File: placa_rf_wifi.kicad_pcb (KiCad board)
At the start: 2 copper layers, 9 parts

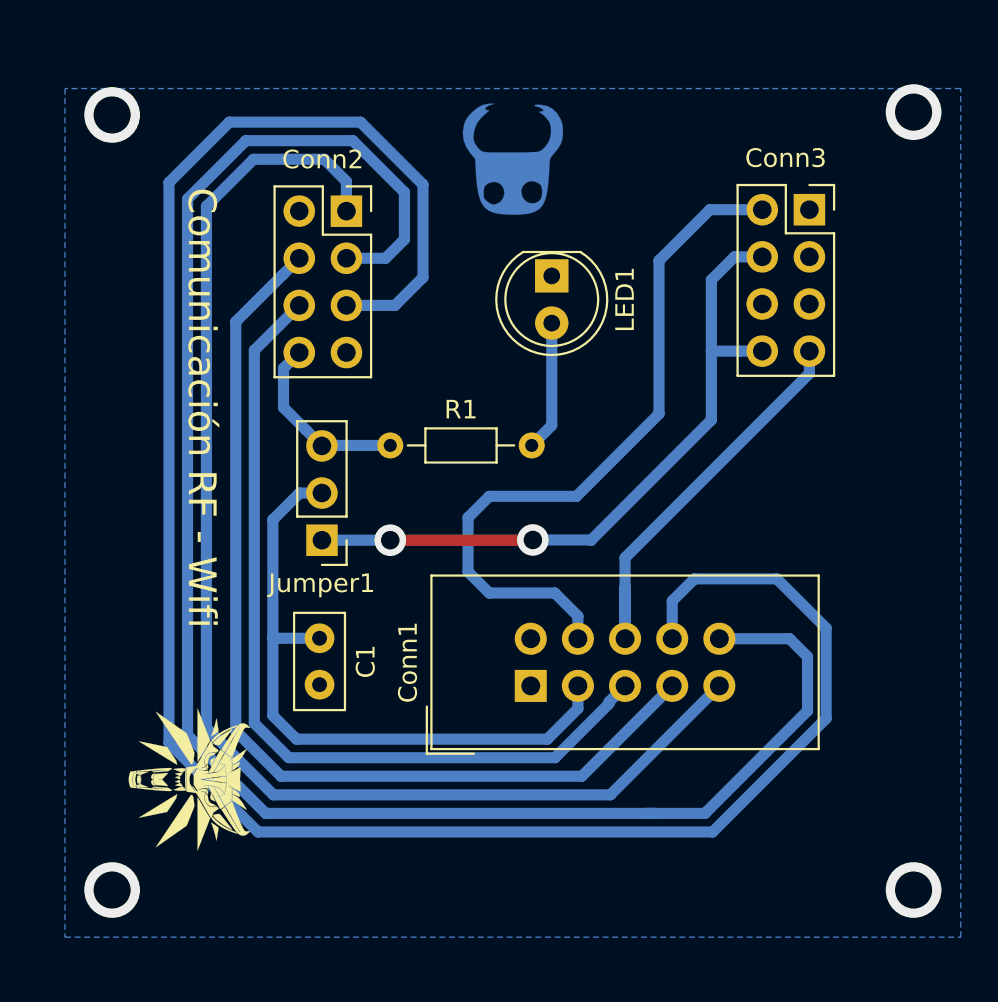
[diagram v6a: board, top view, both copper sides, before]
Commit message: Placa simplificada II, pistas de 1mm
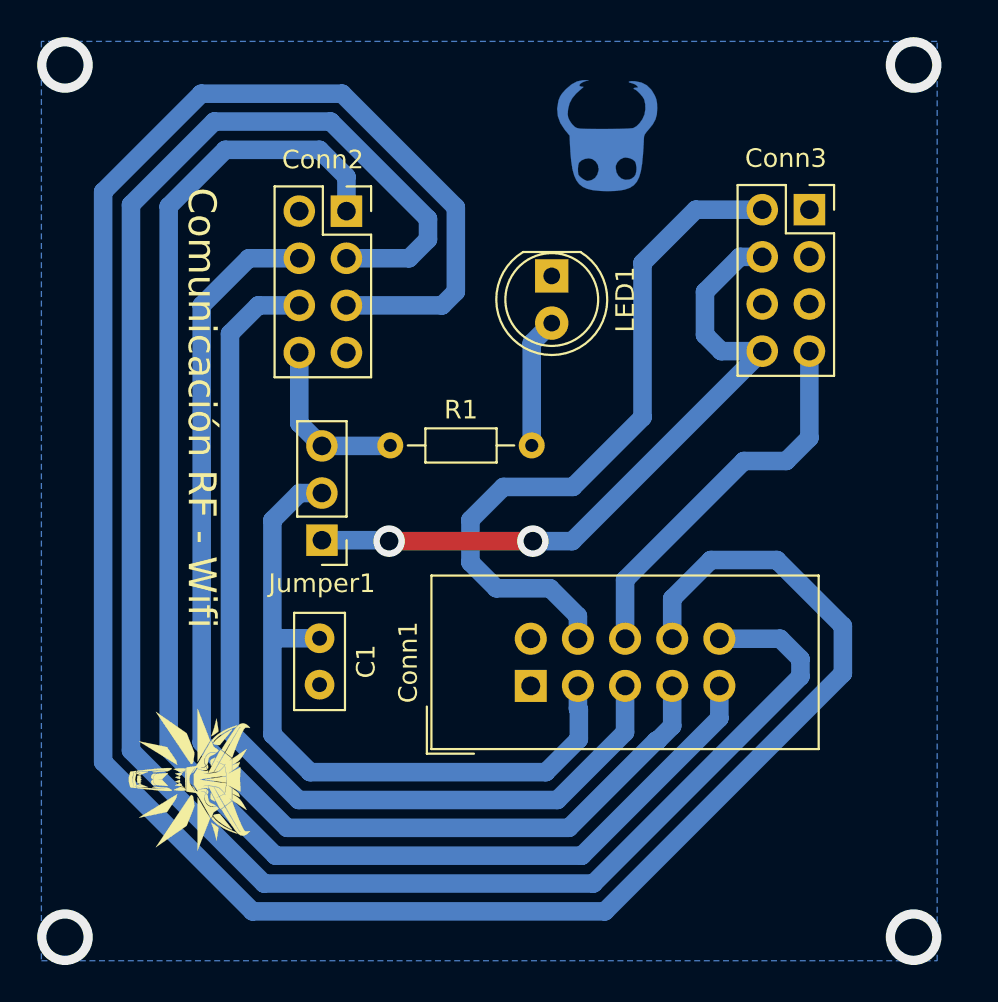
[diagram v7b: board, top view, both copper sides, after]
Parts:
- moved ? 5.24 mm to (143.5, 71.1)
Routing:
- net CE: track 113.1 -> 129.9 mm
- net SCK: track 95.1 -> 104.8 mm
- net MISO: track 70.3 -> 79.4 mm
- net MOSI: track 53.4 -> 61.5 mm
- net CSN: track 45.9 -> 52.6 mm
- net +3V3: track 35.2 -> 38.0 mm
- net RX: track 22.4 -> 20.9 mm
- net VccRF: track 9.93 -> 9.23 mm
- net TX: track 38.6 -> 38.0 mm
- net VccWifi: track 37.0 -> 37.5 mm
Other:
- net class Default: clearance 0.4 -> 0.5; trace_width 0.6 -> 1
- rule trace_clearance: 0.4 -> 0.5

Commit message: Placa simplificada, version final. Se recomienda aumentar el margen entre pistas
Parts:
- added ?: , Logos:Logo_Cobre, F.Cu at (256.5, 129.5)
- added ?: , Logos:Logo_Cobre, F.Cu at (61.0, 129.5)
- added ?: , Logos:Logo_Cobre, F.Cu at (160.0, 129.5)
- added ?: , Logos:Logo_Cobre, F.Cu at (255.3, 44.5)
- added ?: , Logos:Logo_Cobre, F.Cu at (158.8, 44.5)
- added C1: C_Small, Capacitor_THT:C_Disc_D5.0mm_W2.5mm_P2.50mm, F.Cu at (241.0, 156.6)
- added C1: C_Small, Capacitor_THT:C_Disc_D5.0mm_W2.5mm_P2.50mm, F.Cu at (45.5, 156.6)
- added C1: C_Small, Capacitor_THT:C_Disc_D5.0mm_W2.5mm_P2.50mm, F.Cu at (144.5, 156.6)
- added C1: C_Small, Capacitor_THT:C_Disc_D5.0mm_W2.5mm_P2.50mm, F.Cu at (239.8, 71.5)
- added C1: C_Small, Capacitor_THT:C_Disc_D5.0mm_W2.5mm_P2.50mm, F.Cu at (143.3, 71.5)
- added Conn1: Entrada_PIC, Connector_IDC:IDC-Header_2x05_P2.54mm_Vertical, F.Cu at (252.4, 159.2)
- added Conn1: Entrada_PIC, Connector_IDC:IDC-Header_2x05_P2.54mm_Vertical, F.Cu at (155.9, 159.2)
- added Conn1: Entrada_PIC, Connector_IDC:IDC-Header_2x05_P2.54mm_Vertical, F.Cu at (56.8, 159.2)
- added Conn1: Entrada_PIC, Connector_IDC:IDC-Header_2x05_P2.54mm_Vertical, F.Cu at (251.2, 74.1)
- added Conn1: Entrada_PIC, Connector_IDC:IDC-Header_2x05_P2.54mm_Vertical, F.Cu at (154.6, 74.1)
- added Conn2: RF, Conectores_Diseño:PinSocket_2x04_P2.54mm_Vertical, F.Cu at (242.5, 133.6)
- added Conn2: RF, Conectores_Diseño:PinSocket_2x04_P2.54mm_Vertical, F.Cu at (146.0, 133.6)
- added Conn2: RF, Conectores_Diseño:PinSocket_2x04_P2.54mm_Vertical, F.Cu at (46.9, 133.6)
- added Conn2: RF, Conectores_Diseño:PinSocket_2x04_P2.54mm_Vertical, F.Cu at (241.2, 48.5)
- added Conn2: RF, Conectores_Diseño:PinSocket_2x04_P2.54mm_Vertical, F.Cu at (144.7, 48.5)
- added Conn3: Wifi, Conectores_Diseño:PinSocket_2x04_P2.54mm_Vertical_MODIFICADO, F.Cu at (267.4, 133.5)
- added Conn3: Wifi, Conectores_Diseño:PinSocket_2x04_P2.54mm_Vertical_MODIFICADO, F.Cu at (71.9, 133.5)
- added Conn3: Wifi, Conectores_Diseño:PinSocket_2x04_P2.54mm_Vertical_MODIFICADO, F.Cu at (170.9, 133.5)
- added Conn3: Wifi, Conectores_Diseño:PinSocket_2x04_P2.54mm_Vertical_MODIFICADO, F.Cu at (266.2, 48.4)
- added Conn3: Wifi, Conectores_Diseño:PinSocket_2x04_P2.54mm_Vertical_MODIFICADO, F.Cu at (169.6, 48.4)
- added Jumper1: JumperVcc, Connector_PinHeader_2.54mm:PinHeader_1x03_P2.54mm_Vertical, F.Cu at (241.2, 151.3)
- added Jumper1: JumperVcc, Connector_PinHeader_2.54mm:PinHeader_1x03_P2.54mm_Vertical, F.Cu at (45.6, 151.3)
- added Jumper1: JumperVcc, Connector_PinHeader_2.54mm:PinHeader_1x03_P2.54mm_Vertical, F.Cu at (144.7, 151.3)
- added Jumper1: JumperVcc, Connector_PinHeader_2.54mm:PinHeader_1x03_P2.54mm_Vertical, F.Cu at (239.9, 66.2)
- added Jumper1: JumperVcc, Connector_PinHeader_2.54mm:PinHeader_1x03_P2.54mm_Vertical, F.Cu at (143.4, 66.2)
- added LED1: D_Rf, LED_THT:LED_D5.0mm, F.Cu at (253.6, 137.1)
- added LED1: D_Rf, LED_THT:LED_D5.0mm, F.Cu at (58.0, 137.1)
- added LED1: D_Rf, LED_THT:LED_D5.0mm, F.Cu at (157.0, 137.1)
- added LED1: D_Rf, LED_THT:LED_D5.0mm, F.Cu at (252.3, 52.0)
- added LED1: D_Rf, LED_THT:LED_D5.0mm, F.Cu at (155.8, 52.0)
- added R1: R_Rf, Resistor_THT:R_Axial_DIN0204_L3.6mm_D1.6mm_P7.62mm_Horizontal, F.Cu at (244.9, 146.2)
- added R1: R_Rf, Resistor_THT:R_Axial_DIN0204_L3.6mm_D1.6mm_P7.62mm_Horizontal, F.Cu at (49.3, 146.2)
- added R1: R_Rf, Resistor_THT:R_Axial_DIN0204_L3.6mm_D1.6mm_P7.62mm_Horizontal, F.Cu at (148.3, 146.2)
- added R1: R_Rf, Resistor_THT:R_Axial_DIN0204_L3.6mm_D1.6mm_P7.62mm_Horizontal, F.Cu at (243.6, 61.1)
- added R1: R_Rf, Resistor_THT:R_Axial_DIN0204_L3.6mm_D1.6mm_P7.62mm_Horizontal, F.Cu at (147.1, 61.1)
- moved ? 88.0 mm to (59.7, 44.5)
- moved C1 88.0 mm to (44.2, 71.5)
- moved Conn1 88.0 mm to (55.6, 74.1)
- moved Conn2 88.0 mm to (45.6, 48.5)
- moved Conn3 88.0 mm to (70.6, 48.4)
- moved Jumper1 88.0 mm to (44.3, 66.2)
- moved LED1 88.0 mm to (56.7, 52.0)
- moved R1 88.0 mm to (48.0, 61.1)
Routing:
- net (no net): track 0.00 -> 2895.0 mm, vias 4 -> 34
- added copper zone on B.Cu, net (none)
